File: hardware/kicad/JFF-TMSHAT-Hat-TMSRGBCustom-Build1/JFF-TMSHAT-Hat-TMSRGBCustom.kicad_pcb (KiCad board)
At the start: 2 copper layers, 56 x 58 mm, 44 parts, among them J13 AV EXT, J5 RGB, U1 CD74HC4053PWR, U2 LM1881MX/NOPB, U3 MAX4395EUD, U4 TS5A4597DCKR, U5 SN74LVC2G17DCKR, U6 LMH1251MT/NOPB, U7 THS7374IPWR

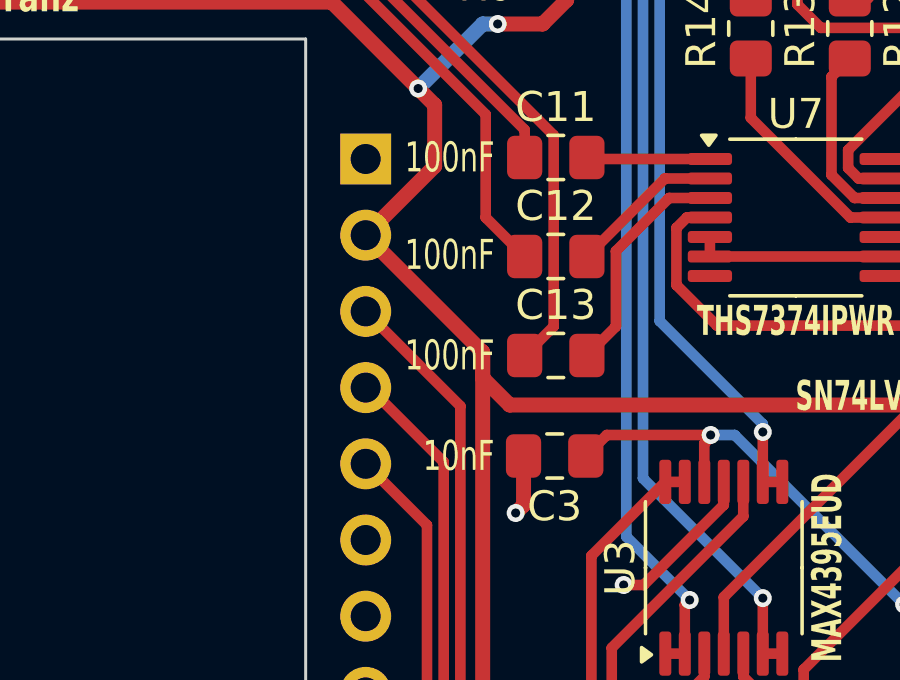
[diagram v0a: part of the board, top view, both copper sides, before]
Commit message: tmshats: add missing Y,R-Y,B-Y resistors
Signed-off-by: Albert Herranz <albert_herranz@yahoo.es>
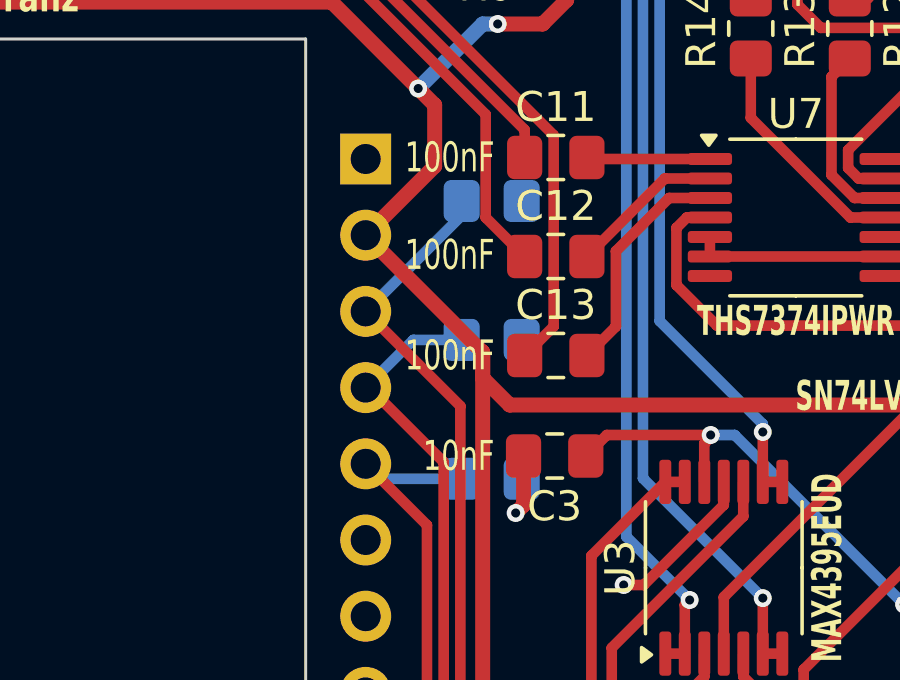
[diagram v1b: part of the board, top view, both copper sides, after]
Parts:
- added R16: 470, Resistor_SMD:R_0805_2012Metric_Pad1.20x1.40mm_HandSolder, B.Cu at (90.1, 99.2)
- added R17: 470, Resistor_SMD:R_0805_2012Metric_Pad1.20x1.40mm_HandSolder, B.Cu at (90.1, 94.5)
- added R18: 470, Resistor_SMD:R_0805_2012Metric_Pad1.20x1.40mm_HandSolder, B.Cu at (90.1, 89.9)
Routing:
- net CPUCLK/R-Y: track 35.0 -> 40.0 mm
- net EXTVDP/B-Y: track 57.0 -> 60.8 mm
- net COMVID/Y: track 33.1 -> 36.5 mm

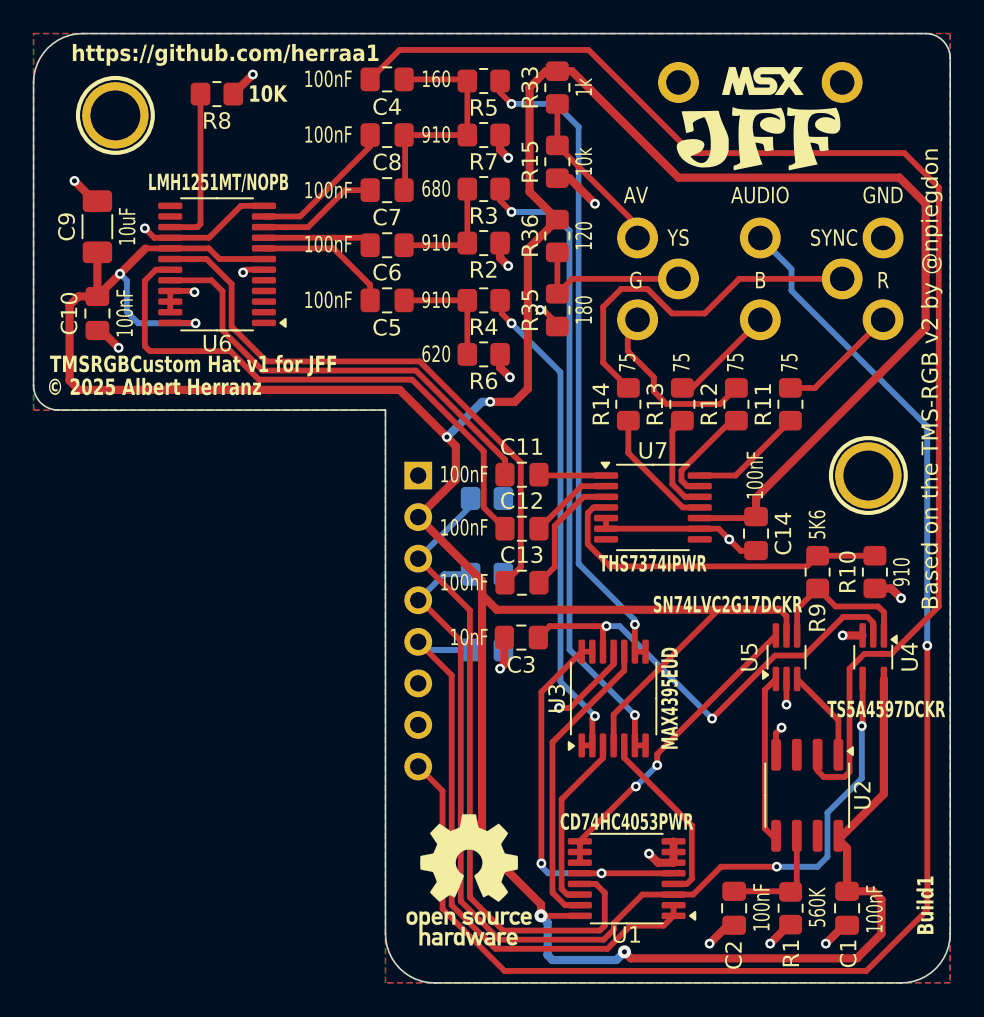
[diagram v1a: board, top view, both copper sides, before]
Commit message: tmshats: re-routed for enhanced reference plane
Signed-off-by: Albert Herranz <albert_herranz@yahoo.es>
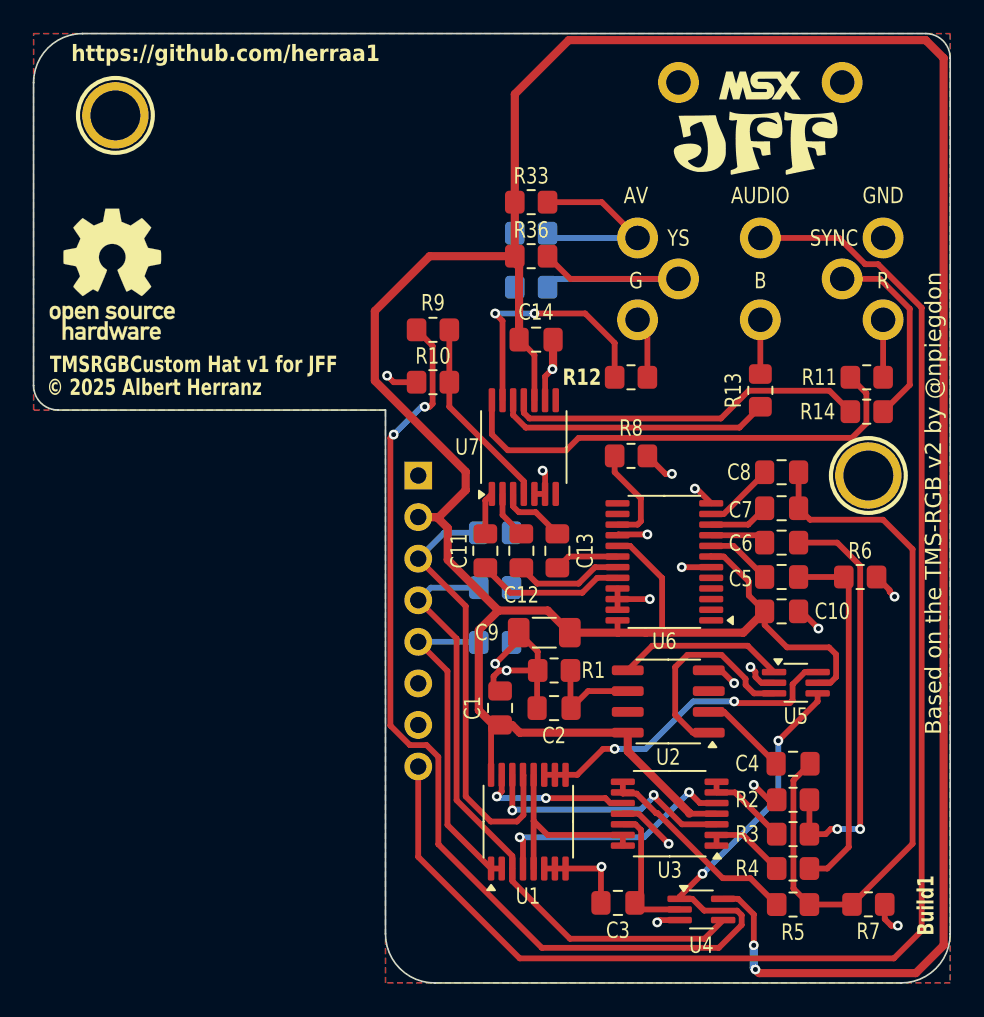
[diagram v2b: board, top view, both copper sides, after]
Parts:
- R15, R35: moved to B.Cu
- moved R5 53.7 mm to (108.8, 114.7), turned to 0 degrees
- moved R7 52.5 mm to (113.4, 114.7)
- moved C4 48.6 mm to (108.8, 106.1)
- moved C10 45.6 mm to (108.1, 96.8), turned to 0 degrees
- moved R3 43.7 mm to (108.8, 110.4), turned to 0 degrees
- moved SYM1 42.9 mm to (67.2, 76.2)
- moved R4 39.5 mm to (108.8, 112.5), turned to 0 degrees
- moved R2 38.9 mm to (108.8, 108.3), turned to 0 degrees
- moved C9 36.9 mm to (93.6, 98.1), turned to 180 degrees
- moved R8 33.6 mm to (98.9, 87.3)
- moved U6 32.8 mm to (100.9, 93.8)
- moved C8 31.7 mm to (108.1, 88.3)
- moved C7 31.0 mm to (108.1, 90.5)
- moved C6 30.2 mm to (108.1, 92.6)
- moved C5 29.4 mm to (108.1, 94.7)
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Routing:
- net Net-(U2-VIDEO_IN): track 81.1 -> 5.43 mm
- net /CSYNC: track 9.46 -> 77.6 mm, vias 0 -> 4
- net Net-(U3-B): track 39.5 -> 5.38 mm, vias 2 -> 0
- net Net-(U6-B_OUT): track 35.8 -> 3.96 mm
- net Net-(C4-Pad1): track 14.5 -> 45.5 mm
- net +5V: track 249.1 -> 220.9 mm, vias 6 -> 2
- net Net-(U6-G_OUT): track 34.5 -> 6.69 mm
- net Net-(U3-C): track 40.5 -> 12.9 mm, vias 2 -> 0
- net Net-(U3-A): track 30.3 -> 5.17 mm, vias 2 -> 0
- net EXTVDP/B-Y: track 60.8 -> 38.4 mm, vias 2 -> 0
- net Net-(U7-CH1OUT): track 6.93 -> 29.3 mm
- net Net-(U3-D+): track 28.2 -> 8.77 mm, vias 2 -> 0
- net Net-(C6-Pad1): track 7.26 -> 25.8 mm, vias 0 -> 2
- net Net-(U6-R_OUT): track 27.3 -> 9.08 mm
- net COMVID/Y: track 36.5 -> 20.1 mm
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- added copper zone on F.Cu, net GND
- removed copper zone on F.Cu, net +5V

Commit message: tmshats: changed logos, minor routing change
Signed-off-by: Albert Herranz <albert_herranz@yahoo.es>
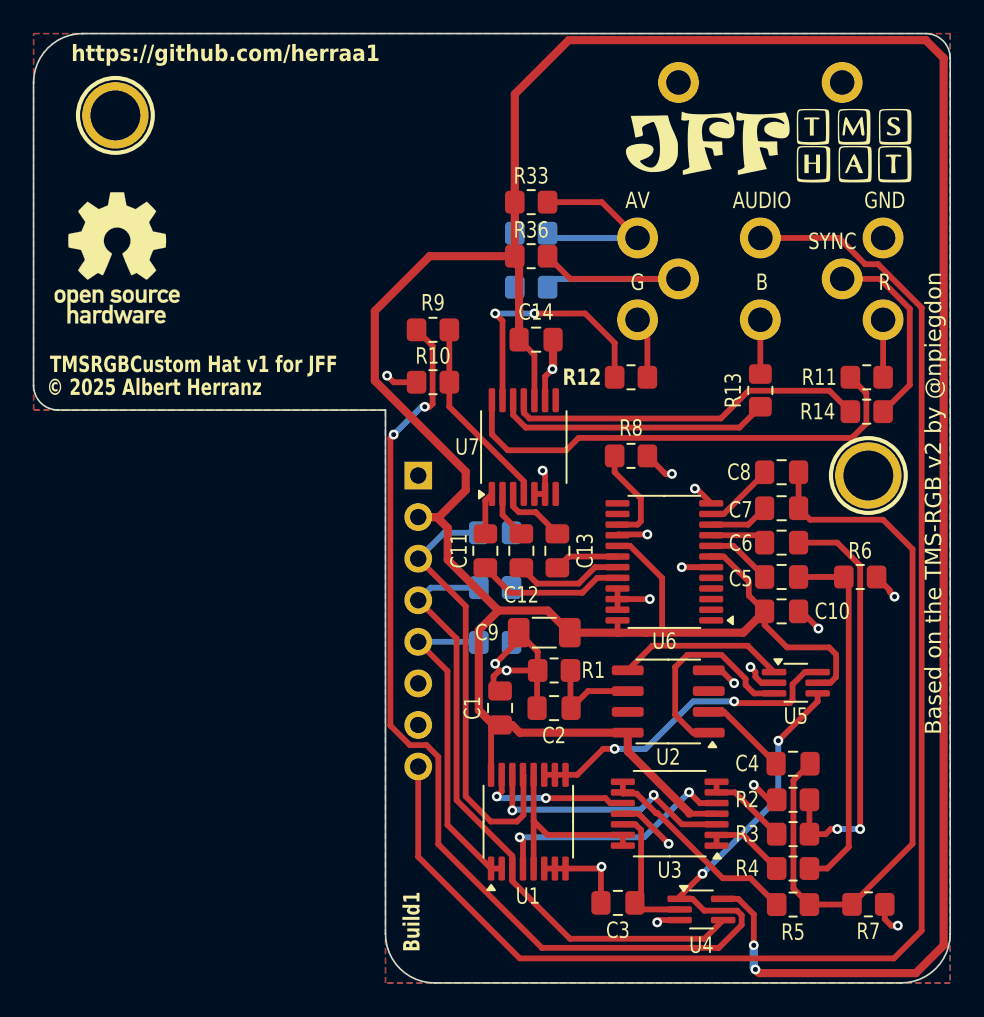
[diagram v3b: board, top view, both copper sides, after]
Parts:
- added G***: LOGO, My_Components:logo-hat, F.Cu at (112.5, 69.5)
- added G***: LOGO, My_Components:logo-tms, F.Cu at (112.5, 67.2)
- moved SYM1 1.04 mm to (67.5, 75.2)
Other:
- board text removed: "YS"

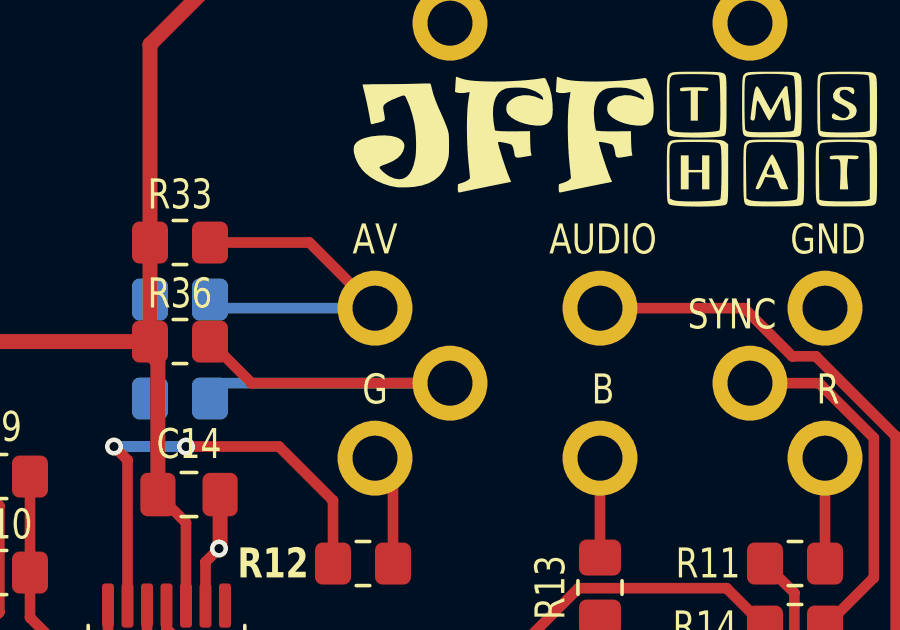
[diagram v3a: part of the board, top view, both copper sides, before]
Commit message: tmshats: add back missing YS silkscreen text
Signed-off-by: Albert Herranz <albert_herranz@yahoo.es>
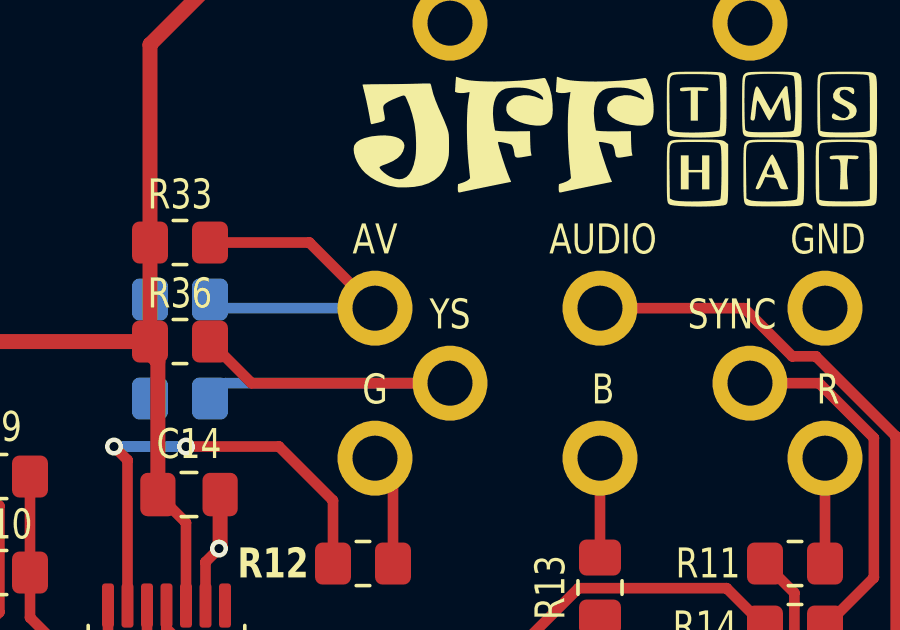
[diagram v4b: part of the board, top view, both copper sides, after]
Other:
- board text added: "YS"
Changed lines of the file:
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@@
 			(fill yes)
 			(layer "F.SilkS")
-			(net 1618966320)
 		)
 		(fp_poly
@@
 			(fill yes)
 			(layer "F.SilkS")
-			(net 1618966320)
 		)
 		(fp_poly
@@
 			(fill yes)
 			(layer "F.SilkS")
-			(net 1618966320)
 		)
 		(fp_poly
@@
 			(fill yes)
 			(layer "F.SilkS")
-			(net 1618966320)
 		)
 		(fp_poly
@@
 			(fill yes)
 			(layer "F.SilkS")
-			(net 1618966320)
 		)
 		(fp_poly
@@
 			(fill yes)
 			(layer "F.SilkS")
-			(net 1618966320)
 		)
 		(embedded_fonts no)
@@
 			(fill yes)
 			(layer "F.SilkS")
-			(net 1618966320)
 		)
 		(fp_poly
@@
 			(fill yes)
 			(layer "F.SilkS")
-			(net 1618966320)
 		)
 		(fp_poly
@@
 			(fill yes)
 			(layer "F.SilkS")
-			(net 1618966320)
 		)
 		(fp_poly
@@
 			(fill yes)
 			(layer "F.SilkS")
-			(net 1618966320)
 		)
 		(fp_poly
@@
 			(fill yes)
 			(layer "F.SilkS")
-			(net 1618966320)
 		)
 		(fp_poly
@@
 			(fill yes)
 			(layer "F.SilkS")
-			(net 1618966320)
 		)
 		(embedded_fonts no)
@@
 		(layer "F.SilkS")
 		(effects
+			(font
+				(size 1 0.8)
+				(thickness 0.2)
+			)
+		)
+	)
+	(gr_text "YS"
+		(at 101.8 74.2 0)
+		(layer "F.SilkS")
+		(effects
